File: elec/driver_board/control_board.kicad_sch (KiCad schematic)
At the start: 12 parts, among them J1 rotary_encoder, J2 DCF77 board, J3 RTC, U1 ESP32-C3-DEVKITM-1, U2 TXB0102DCT

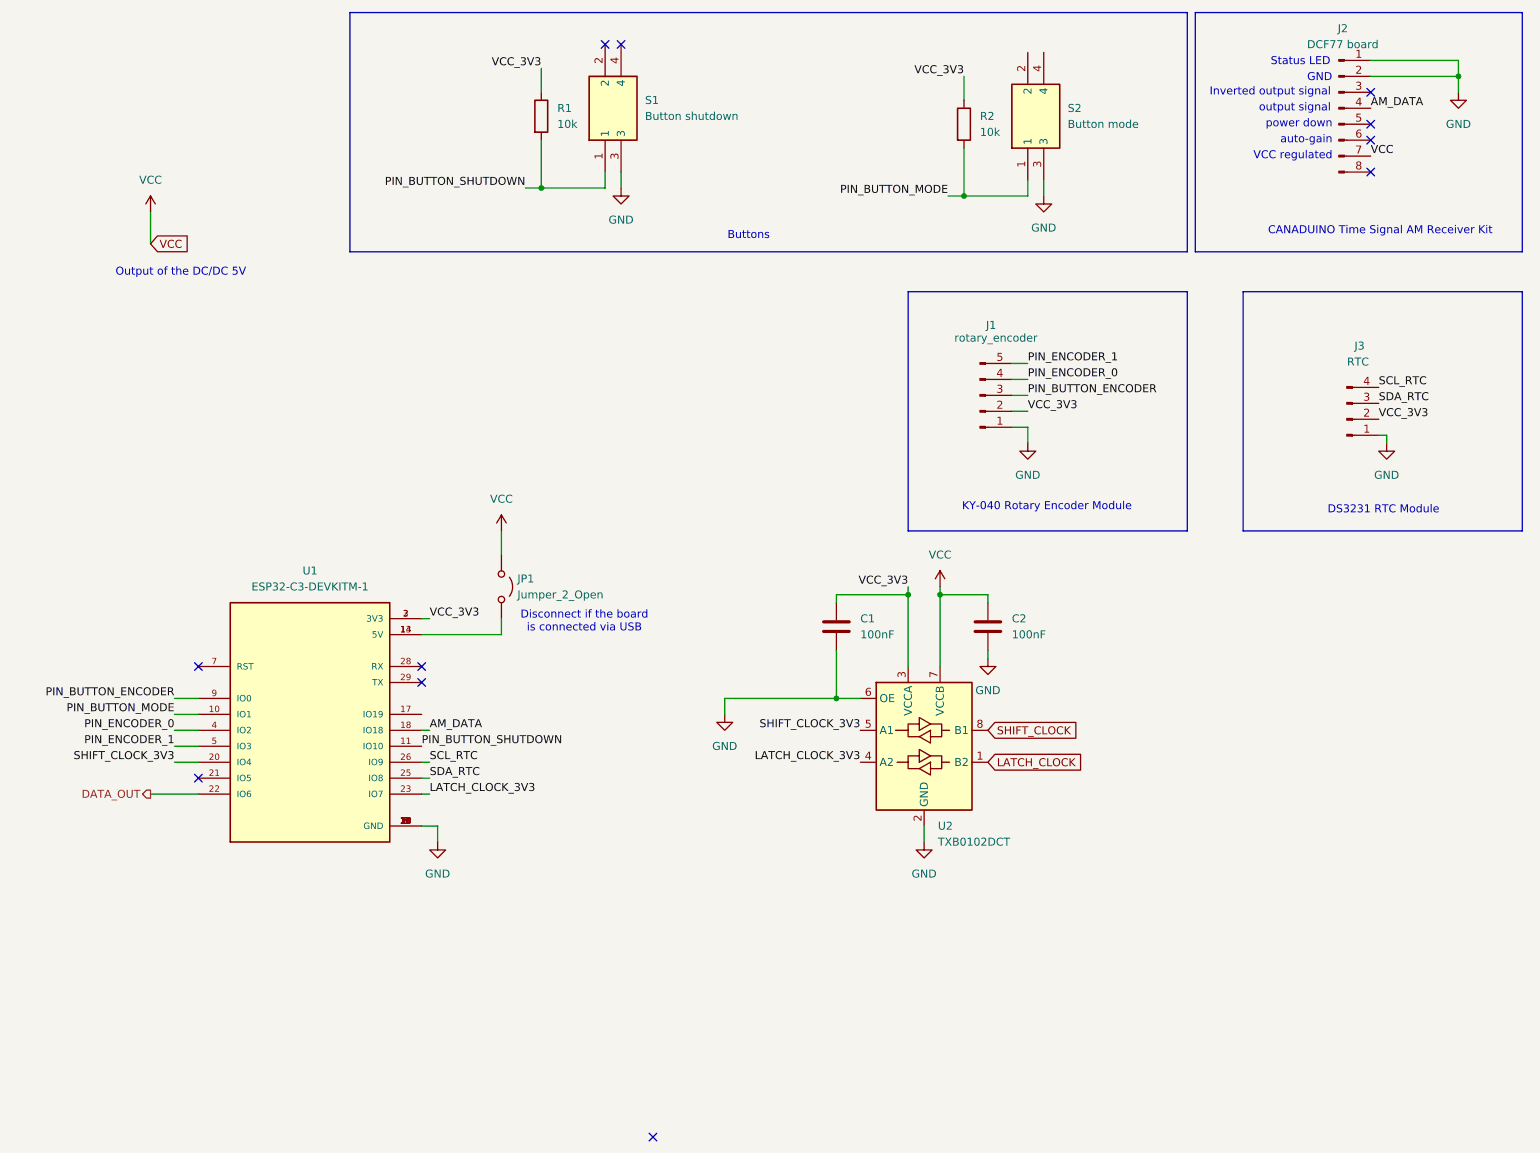
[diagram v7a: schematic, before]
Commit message: PCB done, ready to be ordered
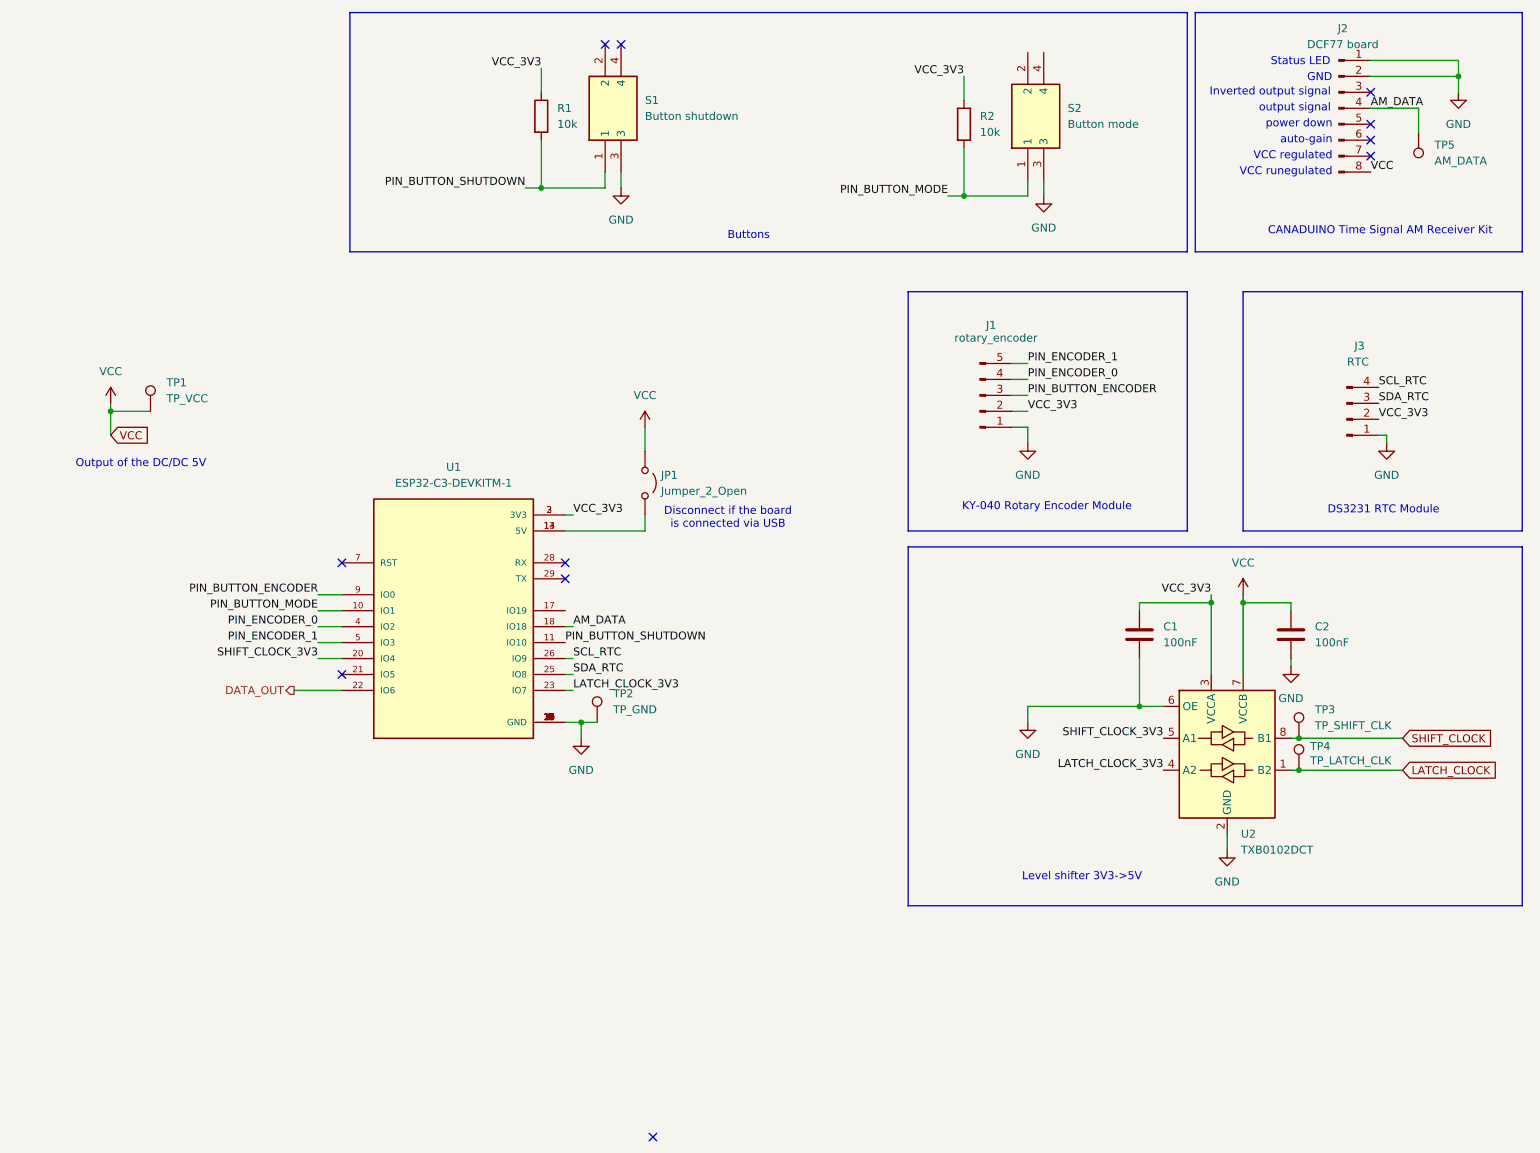
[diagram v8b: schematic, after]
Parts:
- added TP1: TP_VCC, TestPoint:TestPoint_Pad_1.5x1.5mm, symbol Connector:TestPoint
- added TP2: TP_GND, TestPoint:TestPoint_Pad_1.5x1.5mm, symbol Connector:TestPoint
- added TP3: TP_SHIFT_CLK, TestPoint:TestPoint_Pad_2.0x2.0mm, symbol Connector:TestPoint
- added TP4: TP_LATCH_CLK, TestPoint:TestPoint_Pad_2.0x2.0mm, symbol Connector:TestPoint
- added TP5: AM_DATA, TestPoint:TestPoint_Pad_1.5x1.5mm, symbol Connector:TestPoint
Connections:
- net AM_DATA: now also TP5.1
- net GND: now also TP2.1
- net LATCH_CLOCK: now also TP4.1
- net SHIFT_CLOCK: now also TP3.1
- net VCC: now also J2.8 (Pin_8), TP1.1; no longer J2.7 (Pin_7)
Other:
- note added: "Level shifter 3V3->5V"
- note added: "VCC runegulated"
- moved on the sheet: C1, C2, JP1, U1, U2
